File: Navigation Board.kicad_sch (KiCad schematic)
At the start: 137 parts, among them IC1 NEO-M9N-00B, IC2 NRF24L01, IC3 TLV75533PDBVR, IC4 RFX2401C, IC5 TPS61232DRCR, IC6 TPS2115ADRBR, IC7 MCP73833-FCI_MF, IC8 BNO086, J1 UJ20-C-H-G-SMT-5-P16-TR, J2 CONSMA022-G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

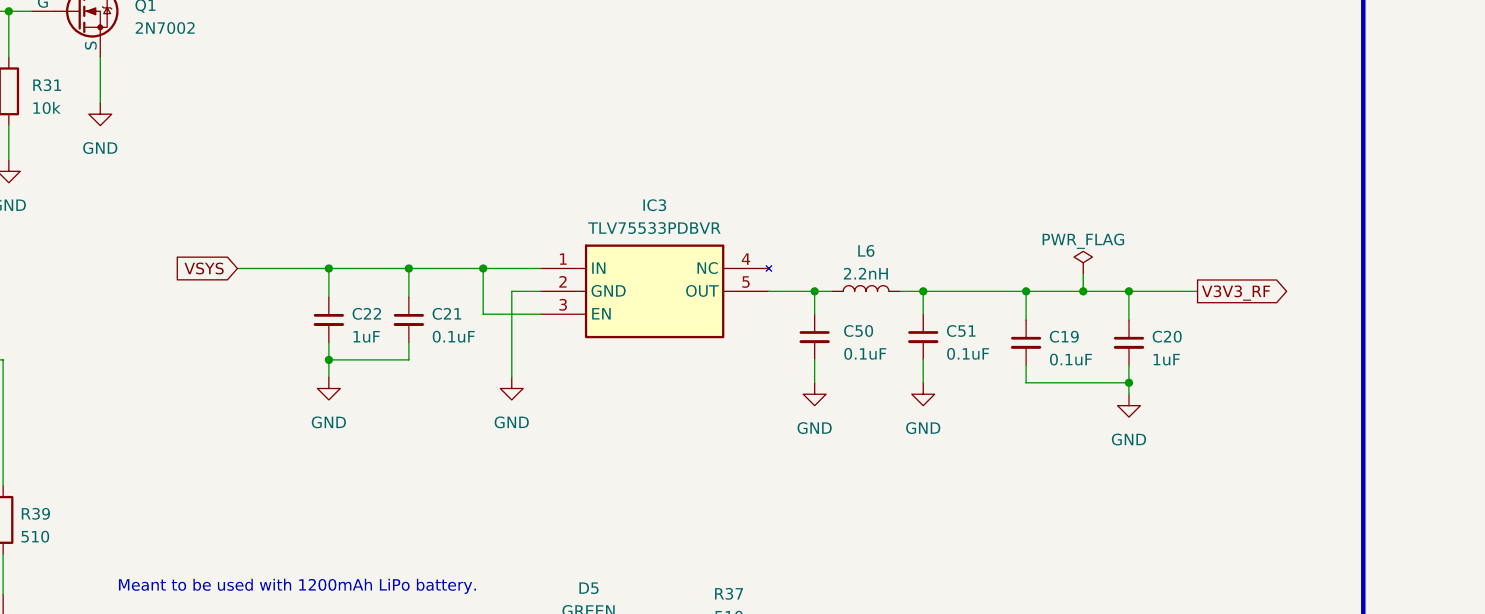
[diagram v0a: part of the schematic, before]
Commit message: Moved pi filter to input of LDO from output. Also added drill table
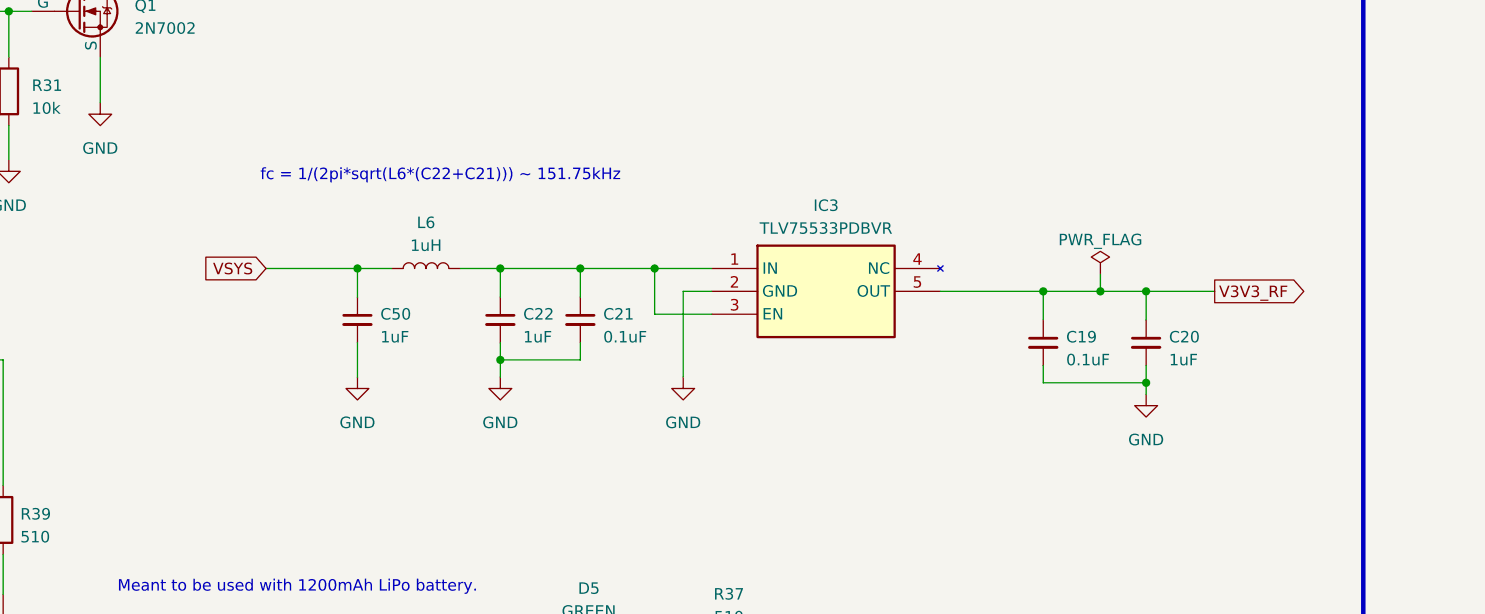
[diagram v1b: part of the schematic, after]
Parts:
- removed C51: 0.1uF, Capacitor_SMD:C_0603_1608Metric, symbol Device:C_Small
- C50: value 0.1uF -> 1uF
- L6: value 2.2nH -> 1uH; footprint Inductor_SMD:L_0402_1005Metric -> Inductor_SMD:L_Vishay_IHLP-1616
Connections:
- net V3V3_RF: now also IC3.5 (OUT); no longer L6.2
- net VSYS: now also C50.1, L6.1; no longer C21.1, C22.1, IC3.1 (IN), IC3.3 (EN)
- new net: C21.1, C22.1, IC3.1 (IN), IC3.3 (EN), L6.2
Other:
- note added: "fc = 1/(2pi*sqrt(L6*(C22+C21))) ~ 151.75kHz"
- moved on the sheet: C19, C20, C21, C22, IC3
